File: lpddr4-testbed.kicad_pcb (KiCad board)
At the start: 6 copper layers, 69.6 x 30 mm, 42 parts, among them J1 ddr4-sodimm-edge-connector, U1 MT53E256M16D1

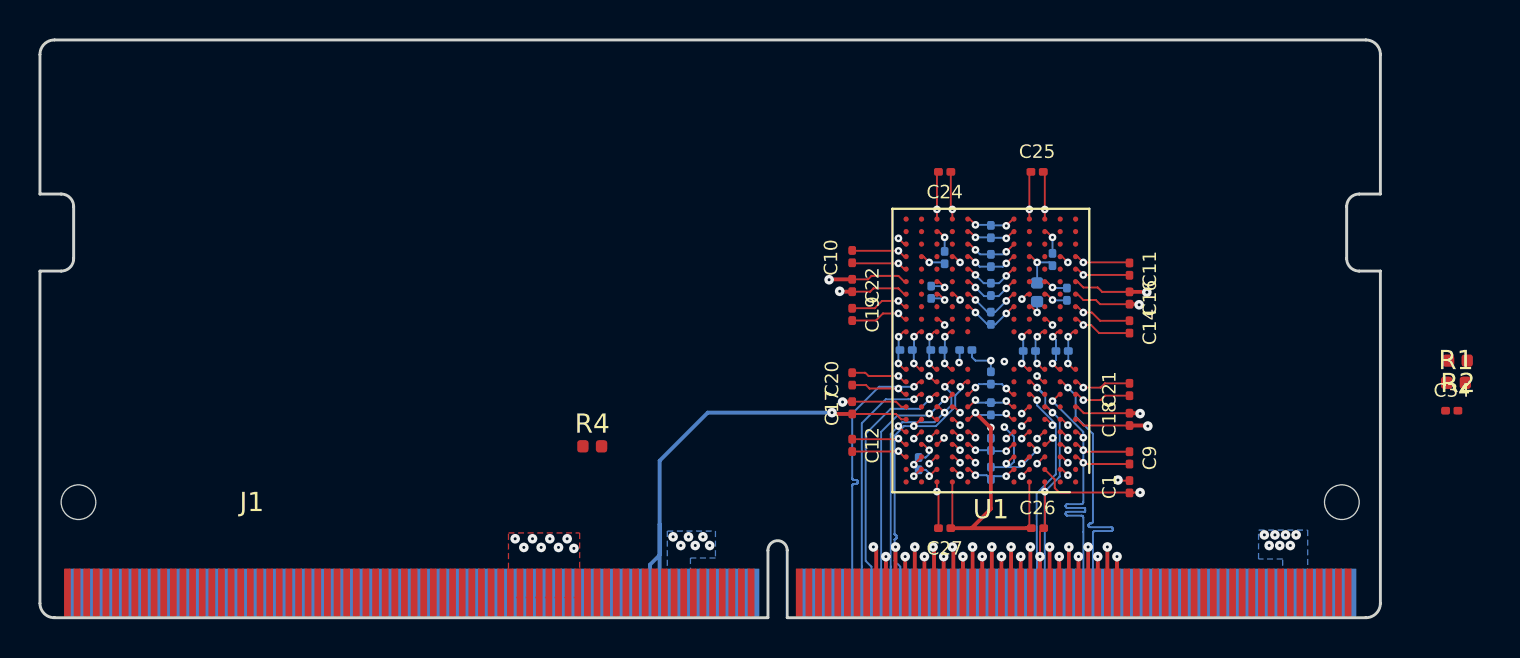
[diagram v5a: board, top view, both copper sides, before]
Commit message: Fully routed, DRC clean
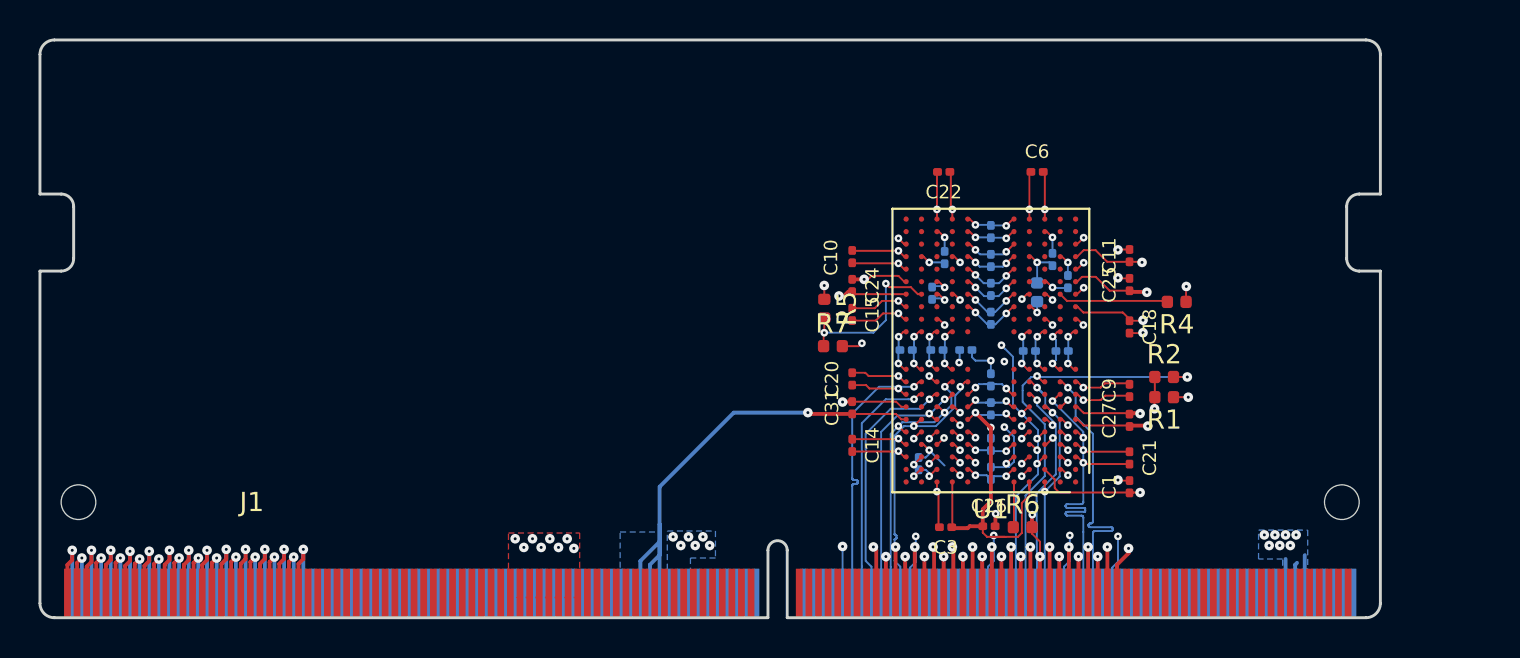
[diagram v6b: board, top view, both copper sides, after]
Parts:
- removed C34: C_100n_0201, antmicro-footprints:0201-res
- added R5: R_10k_0402, antmicro-footprints:0402-res, F.Cu at (140.7, 84.0)
- added R6: R_240R_0402, antmicro-footprints:0402-res, F.Cu at (151.0, 95.3)
- added R7: R_0R_0402, antmicro-footprints:0402-res, F.Cu at (141.2, 85.9)
- C12, C16, C17, C19: moved to B.Cu
- C15, C3, C31, C6: moved to F.Cu
- moved R4 31.3 mm to (159.0, 83.6), turned to 180 degrees
- moved C14 15.7 mm to (142.2, 91.0)
- moved R2 15.3 mm to (158.4, 87.5), turned to 0 degrees
- moved R1 15.2 mm to (158.4, 88.5), turned to 180 degrees
- moved C27 11.1 mm to (156.6, 89.8), turned to 90 degrees
- moved C12 10.4 mm to (151.4, 86.2), turned to 180 degrees
- moved C31 9.66 mm to (142.2, 89.1), turned to 90 degrees
- moved C6 8.33 mm to (151.8, 76.8), turned to 0 degrees
- moved C17 7.96 mm to (149.4, 92.5)
- moved C15 7.73 mm to (142.2, 84.2), turned to 270 degrees
- moved C24 7.61 mm to (142.2, 82.8), turned to 270 degrees
- moved C22 7.57 mm to (146.9, 76.8), turned to 180 degrees
- moved C25 7.57 mm to (156.6, 82.7), turned to 90 degrees
- moved C16 7.46 mm to (149.4, 81.5), turned to 90 degrees
- moved C18 4.80 mm to (156.6, 84.9), turned to 270 degrees
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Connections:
- C12 pad 1: VDDQ -> VDD2
- C14 pad 1: VDD2 -> VDDQ
- C15 pad 1: VDDQ -> VDD2
- C16 pad 1: VDD1 -> VDDQ
- C17 pad 1: VDD1 -> VDDQ
- C18 pad 1: VDD1 -> VDD2
- C19 pad 1: VDD2 -> VDDQ
- C21 pad 1: VDD2 -> VDDQ
- C22 pad 1: VDD1 -> VDD2
- C23 pad 1: VDD1 -> VDD2
- C24 pad 1: VDD2 -> VDD1
- C25 pad 1: VDD2 -> VDD1
- C27 pad 1: VDD2 -> VDD1
- C29 pad 1: VDD2 -> VDD1
- C3 pad 1: VDDQ -> VDD2
- C31 pad 1: VDD2 -> VDD1
- C6 pad 1: VDDQ -> VDD2
- C9 pad 1: VDDQ -> VDD2
- J1 pad 190: Net-(J1-Pad190) -> RESET_N
- J1 pad 192: Net-(J1-Pad192) -> OTD_CA_A
- J1 pad 245: VDD2 -> Net-(J1-Pad245)
- J1 pad 247: VDD2 -> Net-(J1-Pad247)
- J1 pad 249: VDD2 -> Net-(J1-Pad249)
- J1 pad 251: VDD2 -> Net-(J1-Pad251)
- J1 pad 252: VDD1 -> Net-(J1-Pad252)
- J1 pad 253: VDD2 -> Net-(J1-Pad253)
- J1 pad 254: VDD1 -> Net-(J1-Pad254)
- J1 pad 255: VDD2 -> Net-(J1-Pad255)
- J1 pad 256: VDD1 -> Net-(J1-Pad256)
- J1 pad 257: VDD2 -> Net-(J1-Pad257)
- J1 pad 258: VDD1 -> Net-(J1-Pad258)
- J1 pad 259: VDD2 -> Net-(J1-Pad259)
- J1 pad 260: VDD1 -> Net-(J1-Pad260)
- R2 pad 2: /LPDDR4/ODT_CA_A -> OTD_CA_A
- R4 pad 1: Net-(R4-Pad1) -> VDDQ
- U1 pad T2: Net-(U1-PadT2) -> Net-(R4-Pad2)
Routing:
- net GND: track 108.8 -> 220.5 mm, vias 65 -> 101
- net RESET_N: track 0.00 -> 22.4 mm, vias 0 -> 2
- net OTD_CA_A: track 0.00 -> 21.1 mm, vias 0 -> 1
- net Net-(R5-Pad2): track 0.00 -> 8.93 mm, vias 0 -> 2
- net VDDQ: track 35.9 -> 44.4 mm, vias 33 -> 36
- net Net-(R1-Pad2): track 0.00 -> 7.35 mm, vias 0 -> 2
- net Net-(R4-Pad2): track 0.00 -> 5.73 mm
- net Net-(R6-Pad1): track 0.00 -> 2.36 mm
- net VDD2: track 55.3 -> 56.9 mm
- net VDD1: track 87.5 -> 88.4 mm
- added copper zone on In4.Cu, net GND
- added copper zone on B.Cu, net VDD1

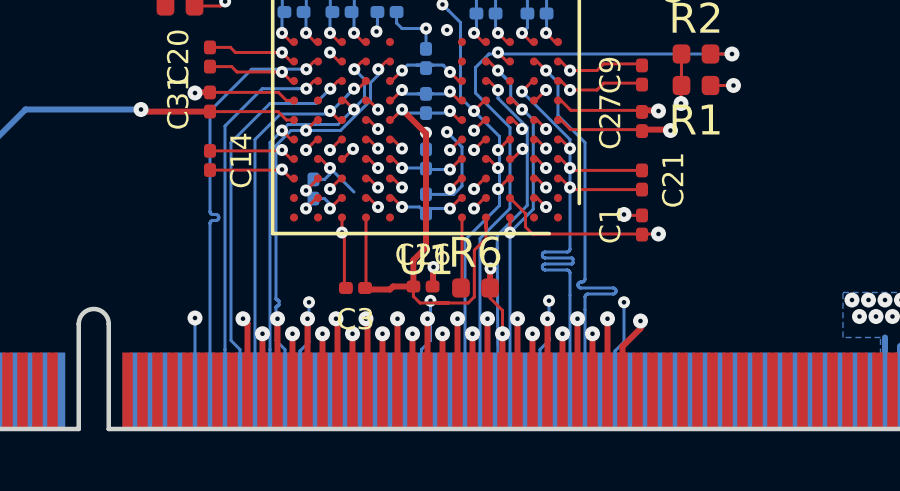
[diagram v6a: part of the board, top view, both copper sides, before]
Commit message: Reconnect RESET_N and ODT_CA to IO_P4 and IO_N5
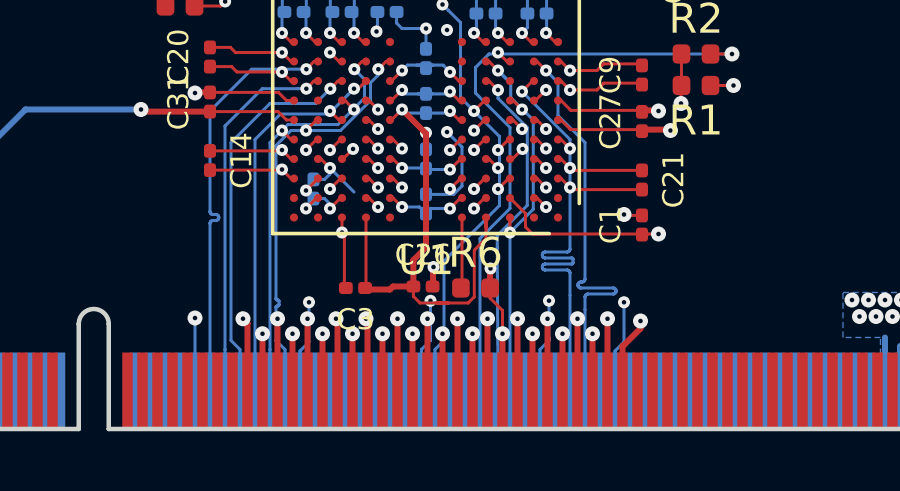
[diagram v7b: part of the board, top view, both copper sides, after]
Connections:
- J1 pad 186: Net-(J1-Pad186) -> RESET_N
- J1 pad 190: RESET_N -> Net-(J1-Pad190)
